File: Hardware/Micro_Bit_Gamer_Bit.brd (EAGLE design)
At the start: 139.7 x 50.8 mm, 15 parts

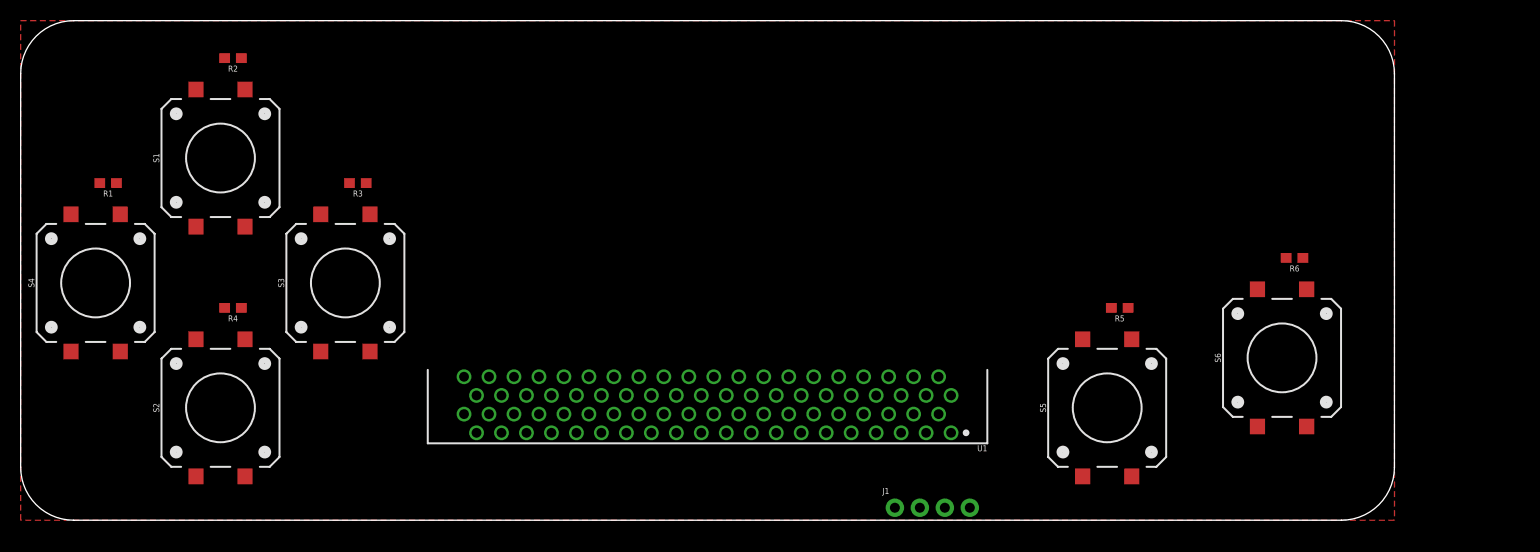
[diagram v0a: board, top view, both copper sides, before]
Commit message: Adding pokehome connectors & a little test code
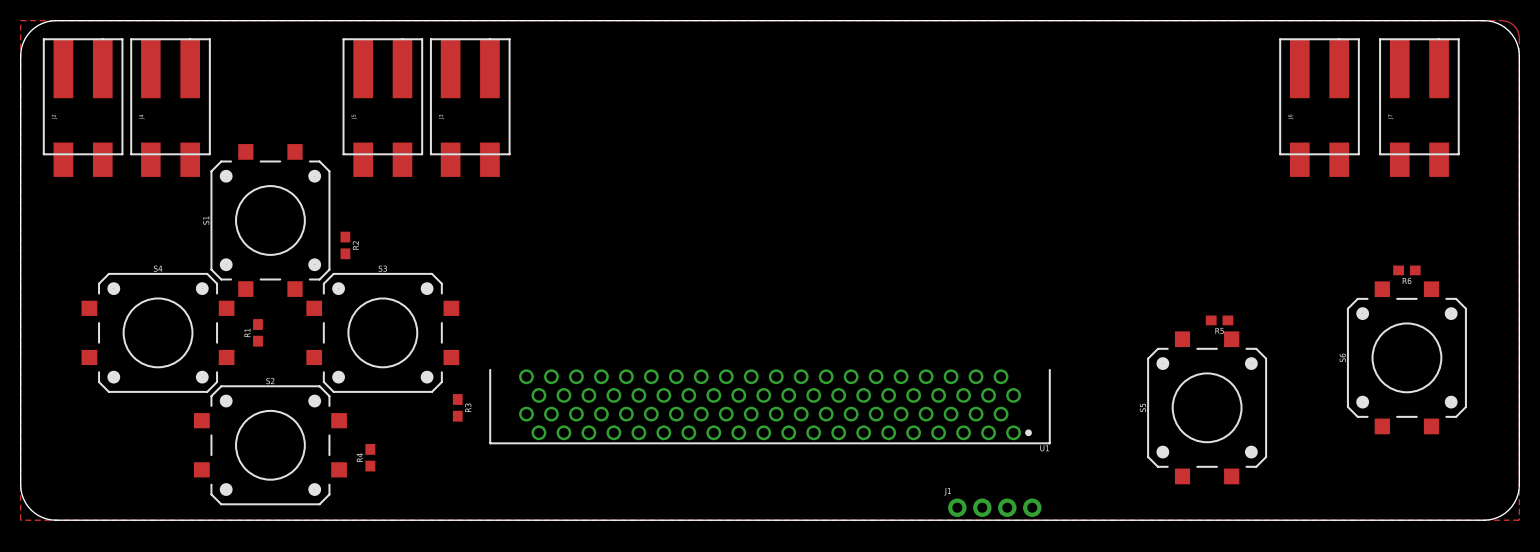
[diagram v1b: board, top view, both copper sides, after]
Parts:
- added J2, J3, J4, J5, J6, J7: (no value), SparkFun-Connectors:1X02_POKEHOME
- J1: value (none) -> I2C
- S1, S2, S3, S4, S5, S6: value TACT-SWITCH -> TACT
- U1: value (none) -> micro:bit
- moved R3 25.0 mm to (44.5, 11.4), turned to 270 degrees
- moved R2 22.2 mm to (33.0, 27.9), turned to 270 degrees
- moved R1 21.6 mm to (24.1, 19.1), turned to 90 degrees
- moved R4 20.7 mm to (35.6, 6.35), turned to 90 degrees
- moved S6 12.7 mm to (141.0, 16.5)
- moved R6 11.5 mm to (141.0, 25.4)
- moved R5 10.2 mm to (121.9, 20.3)
- moved S5 10.2 mm to (120.7, 11.4)
- moved S4 8.13 mm to (14.0, 19.1), turned to 0 degrees
- moved S1 8.13 mm to (25.4, 30.5)
- moved U1 6.35 mm to (76.2, 16.5)
- moved S2 6.35 mm to (25.4, 7.62), turned to 0 degrees
- moved S3 6.35 mm to (36.8, 19.1), turned to 0 degrees
- moved J1 6.35 mm to (95.2, 1.27)
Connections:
- net BTN_A: now also J6.P1, J6.P3
- net BTN_B: now also J7.P1, J7.P3
- net BTN_DN: now also J4.P1, J4.P3
- net BTN_L: now also J5.P1, J5.P3
- net BTN_R: now also J3.P1, J3.P3
- net BTN_UP: now also J2.P1, J2.P3
- net GND: now also J2.P2, J2.P4, J3.P2, J3.P4, J4.P2, J4.P4, J5.P2, J5.P4, J6.P2, J6.P4, J7.P2, J7.P4
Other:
- board size 139.7 x 50.8 mm -> 152.4 x 50.8 mm

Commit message: Board routed, ready for review.
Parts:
- removed J1: I2C, SparkFun-Connectors:1X04_NO_SILK
- added FD1, FD2: FIDUCIALUFIDUCIAL, SparkFun-Aesthetics:FIDUCIAL-MICRO
- added LOGO1: SFE_LOGO_FLAME.5_INCH, SparkFun-Aesthetics:SFE_LOGO_FLAME_.5
- added LOGO2: OSHW-LOGOS, SparkFun-Aesthetics:OSHW-LOGO-S
- added LOGO3: SFE_LOGO_NAME_FLAME.3_INCH, SparkFun-Aesthetics:SFE_LOGO_NAME_FLAME_.3
- J2, J3, J4, J5, J6, J7: value (none) -> Pokehome
- R1, R2, R3, R4, R5, R6: value 100k -> 2.2k
- moved J4 30.5 mm to (45.7, 40.6)
- moved R1 22.2 mm to (43.8, 8.89)
- moved J5 21.6 mm to (15.2, 40.6)
- moved R2 21.6 mm to (41.9, 8.26), turned to 90 degrees
- moved R6 16.3 mm to (128.3, 15.2), turned to 90 degrees
- moved S5 10.6 mm to (114.9, 20.3), turned to 0 degrees
- moved J3 8.98 mm to (36.8, 40.6)
- moved R3 7.75 mm to (38.1, 6.99), turned to 90 degrees
- moved R5 6.75 mm to (126.4, 15.2), turned to 90 degrees
- moved S6 4.96 mm to (137.8, 20.3), turned to 180 degrees
- moved R4 4.62 mm to (40.0, 7.62)
- moved J6 1.80 mm to (133.3, 40.6)
- moved S3 1.42 mm to (37.5, 20.3), turned to 90 degrees
- moved S2 1.42 mm to (26.0, 8.89), turned to 90 degrees
- moved S1 1.42 mm to (26.0, 31.8), turned to 270 degrees
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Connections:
- removed net 3.3V: J1.2, R1.2, R2.2, R3.2, R4.2, R5.2, R6.2, U1.A10, U1.A11, U1.A12, U1.A13, U1.A14, U1.A9
- removed net BTN_A: J6.P1, J6.P3, R5.1, S5.1, U1.A23
- removed net BTN_B: J7.P1, J7.P3, R6.1, S6.1, U1.A15
- removed net SCL: J1.4, U1.A8
- removed net SDA: J1.3, U1.A7
- new net BTN_P12: R5.1, U1.A23
- new net BTN_P16: R6.1, U1.A15
- new net N$1: J2.P2, J2.P4, R1.2, S1.3
- new net N$2: J5.P2, J5.P4, R2.2, S4.3
- new net N$3: J4.P2, J4.P4, R4.2, S2.3
- new net N$4: J3.P2, J3.P4, R3.2, S3.3
- new net N$5: J7.P2, J7.P4, R6.2, S6.3
- new net N$80: J6.P2, J6.P4, R5.2, S5.3
- net BTN_DN: no longer J4.P1, J4.P3, S2.1
- net BTN_L: now also R2.1; no longer J5.P1, J5.P3, R1.1, S4.1
- net BTN_R: no longer J3.P1, J3.P3, S3.1
- net BTN_UP: now also R1.1; no longer J2.P1, J2.P3, R2.1, S1.1
- net GND: now also J2.P1, J2.P3, J3.P1, J3.P3, J4.P1, J4.P3, J5.P1, J5.P3, J6.P1, J6.P3, J7.P1, J7.P3, S1.1, S2.1, S3.1, S4.1, S5.1, S6.1; no longer J1.1, J2.P2, J2.P4, J3.P2, J3.P4, J4.P2, J4.P4, J5.P2, J5.P4, J6.P2, J6.P4, J7.P2, J7.P4, S1.3, S2.3, S3.3, S4.3, S5.3, S6.3
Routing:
- net N$1: track 0.00 -> 78.1 mm, vias 0 -> 3
- net GND: track 0.00 -> 76.6 mm, vias 0 -> 46
- net N$2: track 0.00 -> 68.3 mm, vias 0 -> 2
- net N$3: track 0.00 -> 63.0 mm, vias 0 -> 2
- net BTN_P12: track 0.00 -> 62.1 mm, vias 0 -> 1
- net BTN_P16: track 0.00 -> 55.2 mm, vias 0 -> 1
- net BTN_R: track 0.00 -> 44.5 mm
- net N$4: track 0.00 -> 38.2 mm
- net N$5: track 0.00 -> 37.6 mm
- net N$80: track 0.00 -> 35.1 mm
- net BTN_DN: track 0.00 -> 31.6 mm
- net BTN_L: track 0.00 -> 24.3 mm
- net BTN_UP: track 0.00 -> 14.9 mm
- added copper zone on layer 1, net 3.3V
- added copper zone on layer 16, net 3.3V
- added copper zone on layer 1, net BTN_L
- added copper zone on layer 16, net BTN_L
- added copper zone on layer 1, net BTN_R
- added copper zone on layer 16, net BTN_R
- added copper zone on layer 1, net BTN_UP
- added copper zone on layer 16, net BTN_UP
- added copper zone on layer 16, net GND
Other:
- board text added: "All dimensions in inches."
- board text added: "P0"
- board text added: "P1"
- board text added: "P12"
- board text added: "P16"
- board text added: "P2"
- board text added: "P8"
- board text added: "V01"
- board text added: "gamer:bit"

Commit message: Updates after review.
See review minutes attached to bug for details.
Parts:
- added FD3, FD4: FIDUCIALUFIDUCIAL, SparkFun-Aesthetics:FIDUCIAL-MICRO
- added H1, H2, H3: STAND-OFF, SparkFun-Hardware:STAND-OFF
- added J1, J8: Pokehome, SparkFun-Connectors:1X02_POKEHOME
- added R7, R8: 2.2k, SparkFun-Resistors:0603
- added U$1: SPECIAL_INSTRUCTIONS-ORDERING, SparkFun-Aesthetics:ORDERING_INSTRUCTIONS
- moved FRAME1 23.0 mm to (32.4, -36.2)
- moved LOGO1 10.5 mm to (121.8, 34.8)
- moved S2 5.08 mm to (26.0, 14.0)
- moved S1 5.08 mm to (26.0, 36.8)
- moved S3 5.08 mm to (37.5, 25.4)
- moved S4 5.08 mm to (14.6, 25.4)
- moved S5 5.08 mm to (114.9, 25.4)
- moved S6 5.08 mm to (137.8, 25.4)
- moved R1 4.45 mm to (43.8, 13.3)
- moved R3 4.44 mm to (38.1, 11.4)
- moved R4 4.44 mm to (40.0, 12.1)
- moved R2 4.44 mm to (41.9, 12.7)
- moved J6 3.86 mm to (137.2, 41.3)
- moved J7 3.86 mm to (146.1, 41.3)
- moved LOGO3 2.54 mm to (92.7, 20.3)
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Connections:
- new net BTN_A: R7.1, U1.A34
- new net BTN_B: R8.1, U1.A24
- new net N$6: J8.P2, J8.P4, R8.2
- new net N$7: J1.P2, J1.P4, R7.2
- net GND: now also J1.P1, J1.P3, J8.P1, J8.P3
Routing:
- net BTN_A: track 0.00 -> 92.1 mm, vias 0 -> 3
- net BTN_B: track 0.00 -> 68.2 mm, vias 0 -> 1
- net N$6: track 0.00 -> 39.6 mm
- net GND: track 76.6 -> 58.4 mm, vias 46 -> 47
- net N$7: track 0.00 -> 12.7 mm
- net N$80: track 35.1 -> 40.2 mm
- net N$3: track 63.0 -> 57.9 mm
- net BTN_UP: track 14.9 -> 19.4 mm
- net BTN_R: track 44.5 -> 49.0 mm
- net BTN_L: track 24.3 -> 28.8 mm
- net BTN_DN: track 31.6 -> 36.0 mm
- net N$2: track 68.3 -> 64.5 mm
- net N$5: track 37.6 -> 40.2 mm
- net N$1: track 78.1 -> 75.6 mm
- net N$4: track 38.2 -> 35.6 mm
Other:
- outline, holes or cut-outs redrawn
- board text added: "1. Gloss black soldermask"
- board text added: "3x 0.130 diam holes Clear 4-40 machine screws"
- board text added: "A"
- board text added: "B"
- board text added: "ROUTE OUT"

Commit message: Engineering checklist touchups.
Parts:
- moved FD4 4.58 mm to (151.1, 43.2)
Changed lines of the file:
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@@
 <setting verticaltext="up"/>
 </settings>
-<grid distance="0.1" unitdist="inch" unit="inch" style="lines" multiple="1" display="yes" altdistance="0.01" altunitdist="inch" altunit="inch"/>
+<grid distance="0.025" unitdist="inch" unit="inch" style="lines" multiple="1" display="yes" altdistance="0.005" altunitdist="inch" altunit="inch"/>
 <layers>
 <layer number="1" name="Top" color="4" fill="1" visible="yes" active="yes"/>
@@
 <layer number="20" name="Dimension" color="15" fill="1" visible="yes" active="yes"/>
 <layer number="21" name="tPlace" color="16" fill="1" visible="yes" active="yes"/>
-<layer number="22" name="bPlace" color="14" fill="1" visible="no" active="yes"/>
+<layer number="22" name="bPlace" color="14" fill="1" visible="yes" active="yes"/>
 <layer number="23" name="tOrigins" color="15" fill="1" visible="yes" active="yes"/>
-<layer number="24" name="bOrigins" color="15" fill="1" visible="no" active="yes"/>
-<layer number="25" name="tNames" color="7" fill="1" visible="yes" active="yes"/>
+<layer number="24" name="bOrigins" color="15" fill="1" visible="yes" active="yes"/>
+<layer number="25" name="tNames" color="7" fill="1" visible="no" active="yes"/>
 <layer number="26" name="bNames" color="7" fill="1" visible="no" active="yes"/>
 <layer number="27" name="tValues" color="7" fill="1" visible="no" active="yes"/>
@@
 <layer number="37" name="tTest" color="7" fill="1" visible="no" active="yes"/>
 <layer number="38" name="bTest" color="7" fill="1" visible="no" active="yes"/>
-<layer number="39" name="tKeepout" color="4" fill="11" visible="no" active="yes"/>
-<layer number="40" name="bKeepout" color="1" fill="11" visible="no" active="yes"/>
+<layer number="39" name="tKeepout" color="4" fill="11" visible="yes" active="yes"/>
+<layer number="40" name="bKeepout" color="1" fill="11" visible="yes" active="yes"/>
 <layer number="41" name="tRestrict" color="4" fill="10" visible="no" active="yes"/>
 <layer number="42" name="bRestrict" color="1" fill="10" visible="no" active="yes"/>
 <layer number="43" name="vRestrict" color="2" fill="10" visible="no" active="yes"/>
 <layer number="44" name="Drills" color="7" fill="1" visible="no" active="yes"/>
-<layer number="45" name="Holes" color="7" fill="1" visible="no" active="yes"/>
+<layer number="45" name="Holes" color="7" fill="1" visible="yes" active="yes"/>
 <layer number="46" name="Milling" color="3" fill="1" visible="no" active="yes"/>
-<layer number="47" name="Measures" color="7" fill="1" visible="yes" active="yes"/>
+<layer number="47" name="Measures" color="7" fill="1" visible="no" active="yes"/>
 <layer number="48" name="Document" color="7" fill="1" visible="no" active="yes"/>
 <layer number="49" name="Reference" color="7" fill="1" visible="no" active="yes"/>
@@
 <element name="H3" library="SparkFun-Hardware" package="STAND-OFF" value="STAND-OFF" x="147.32" y="5.08"/>
 <element name="FD3" library="SparkFun-Aesthetics" package="FIDUCIAL-MICRO" value="FIDUCIALUFIDUCIAL" x="2.54" y="10.16" rot="MR0"/>
-<element name="FD4" library="SparkFun-Aesthetics" package="FIDUCIAL-MICRO" value="FIDUCIALUFIDUCIAL" x="147.32" y="40.64" rot="MR0"/>
+<element name="FD4" library="SparkFun-Aesthetics" package="FIDUCIAL-MICRO" value="FIDUCIALUFIDUCIAL" x="151.13" y="43.18" rot="MR0"/>
 </elements>
 <signals>
@@
 <contactref element="R5" pad="2"/>
 <wire x1="135.16" y1="45.275" x2="135.16" y2="36.025" width="0.254" layer="1"/>
-<wire x1="126.365" y1="16.09" x2="126.365" y2="27.9" width="0.254" layer="1"/>
-<wire x1="121.91" y1="27.9" x2="126.325" y2="27.9" width="0.254" layer="1"/>
-<wire x1="126.325" y1="27.9" x2="128.905" y2="30.48" width="0.254" layer="1"/>
 <wire x1="128.905" y1="30.48" x2="133.985" y2="30.48" width="0.254" layer="1"/>
 <wire x1="135.16" y1="36.025" x2="135.16" y2="31.655" width="0.254" layer="1"/>
 <wire x1="135.16" y1="31.655" x2="133.985" y2="30.48" width="0.254" layer="1"/>
-<wire x1="126.365" y1="27.9" x2="126.325" y2="27.9" width="0" layer="19" extent="1-1"/>
+<wire x1="128.905" y1="30.48" x2="126.365" y2="27.94" width="0.254" layer="1"/>
+<wire x1="126.365" y1="27.94" x2="126.365" y2="16.09" width="0.254" layer="1"/>
+<wire x1="121.91" y1="27.9" x2="126.325" y2="27.9" width="0.254" layer="1"/>
+<wire x1="126.325" y1="27.9" x2="126.365" y2="27.94" width="0.254" layer="1"/>
 </signal>
 <signal name="N$5">
